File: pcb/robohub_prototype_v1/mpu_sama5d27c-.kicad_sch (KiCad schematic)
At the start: 9 parts, among them U1 ATSAMA5D27C, Y1 Crystal_GND23_Small

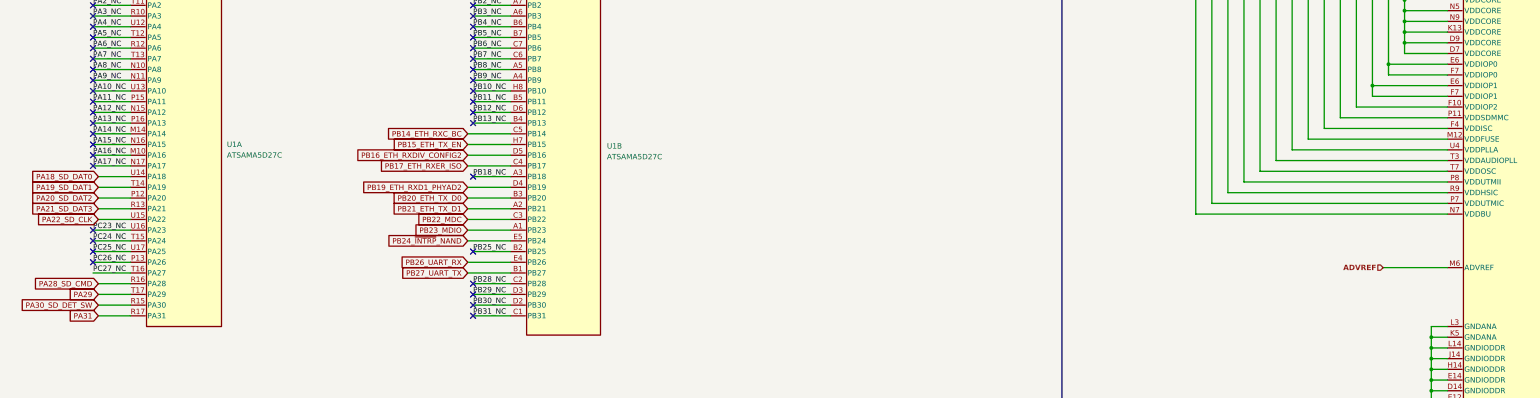
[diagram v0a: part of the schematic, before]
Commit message: Update project to Kicad8. Update schematic, start fanning out BGA on PCB
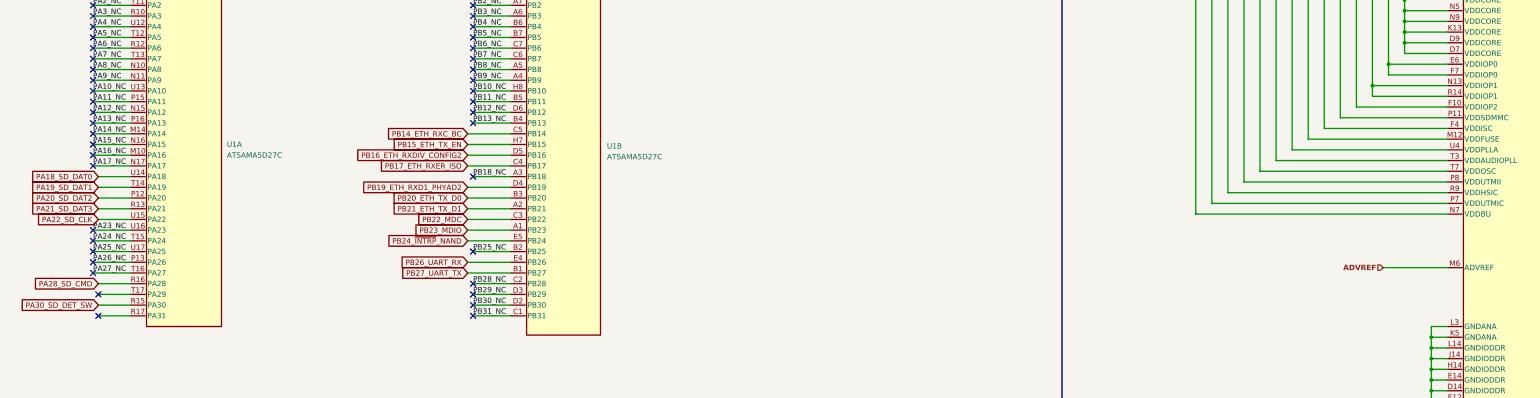
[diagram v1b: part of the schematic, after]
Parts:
- U1: symbol MicroChip_MPU:ATSAMA5D27C -> fryelabs_kicad_symbol_lib:ATSAMA5D27C
- U1: footprint (none) -> custom_footprint:SAMA5D27C-CNVAO
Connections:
- net PC23_NC: no longer U1.U16 (PA23)
- net PC24_NC: no longer U1.T15 (PA24)
- net PC25_NC: no longer U1.U17 (PA25)
- net PC26_NC: no longer U1.P13 (PA26)
- net PC27_NC: no longer U1.T16 (PA27)
- net VDDIOP1: now also U1.N13 (VDDIOP1), U1.R14 (VDDIOP1); no longer U1.E6 (VDDIOP1), U1.F7 (VDDIOP1)
- net PA29: no longer names the net of U1.T17 (PA29)
- net PA31: no longer names the net of U1.R17 (PA31)
- new net PA23_NC: U1.U16 (PA23)
- new net PA24_NC: U1.T15 (PA24)
- new net PA25_NC: U1.U17 (PA25)
- new net PA26_NC: U1.P13 (PA26)
- new net PA27_NC: U1.T16 (PA27)
- no-connect marks 122 -> 125

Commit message: Update paths to footprint libraries. Begin adding footprints for PDN resistors. Create master BOM
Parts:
- U1: footprint custom_footprint:SAMA5D27C-CNVAO -> fryelabs:ATSAMA5D27C
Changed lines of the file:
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@@
 			)
 		)
-		(property "Footprint" "custom_footprint:SAMA5D27C-CNVAO"
+		(property "Footprint" "fryelabs:ATSAMA5D27C"
 			(at 372.618 362.204 0)
 			(effects
@@
 			)
 		)
-		(property "Footprint" "custom_footprint:SAMA5D27C-CNVAO"
+		(property "Footprint" "fryelabs:ATSAMA5D27C"
 			(at 386.588 183.134 0)
 			(effects
@@
 			)
 		)
-		(property "Footprint" "custom_footprint:SAMA5D27C-CNVAO"
+		(property "Footprint" "fryelabs:ATSAMA5D27C"
 			(at 61.468 256.794 0)
 			(effects
@@
 			)
 		)
-		(property "Footprint" "custom_footprint:SAMA5D27C-CNVAO"
+		(property "Footprint" "fryelabs:ATSAMA5D27C"
 			(at 150.368 150.114 0)
 			(effects
@@
 			)
 		)
-		(property "Footprint" "custom_footprint:SAMA5D27C-CNVAO"
+		(property "Footprint" "fryelabs:ATSAMA5D27C"
 			(at 58.928 153.924 0)
 			(effects
@@
 			)
 		)
-		(property "Footprint" "custom_footprint:SAMA5D27C-CNVAO"
+		(property "Footprint" "fryelabs:ATSAMA5D27C"
 			(at 142.748 258.064 0)
 			(effects

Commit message: Begin PDN circuit design/BOM/layout
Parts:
- U1: footprint fryelabs:ATSAMA5D27C -> fryelabs_kicad_footprint_lib:ATSAMA5D27C
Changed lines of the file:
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@@
 			)
 		)
-		(property "Footprint" "fryelabs:ATSAMA5D27C"
+		(property "Footprint" "fryelabs_kicad_footprint_lib:ATSAMA5D27C"
 			(at 372.618 362.204 0)
 			(effects
@@
 			)
 		)
-		(property "Footprint" "fryelabs:ATSAMA5D27C"
+		(property "Footprint" "fryelabs_kicad_footprint_lib:ATSAMA5D27C"
 			(at 386.588 183.134 0)
 			(effects
@@
 			)
 		)
-		(property "Footprint" "fryelabs:ATSAMA5D27C"
+		(property "Footprint" "fryelabs_kicad_footprint_lib:ATSAMA5D27C"
 			(at 61.468 256.794 0)
 			(effects
@@
 			)
 		)
-		(property "Footprint" "fryelabs:ATSAMA5D27C"
+		(property "Footprint" "fryelabs_kicad_footprint_lib:ATSAMA5D27C"
 			(at 150.368 150.114 0)
 			(effects
@@
 			)
 		)
-		(property "Footprint" "fryelabs:ATSAMA5D27C"
+		(property "Footprint" "fryelabs_kicad_footprint_lib:ATSAMA5D27C"
 			(at 58.928 153.924 0)
 			(effects
@@
 			)
 		)
-		(property "Footprint" "fryelabs:ATSAMA5D27C"
+		(property "Footprint" "fryelabs_kicad_footprint_lib:ATSAMA5D27C"
 			(at 142.748 258.064 0)
 			(effects
